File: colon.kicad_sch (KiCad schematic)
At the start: 10 parts, among them U42 SN74LVC244A

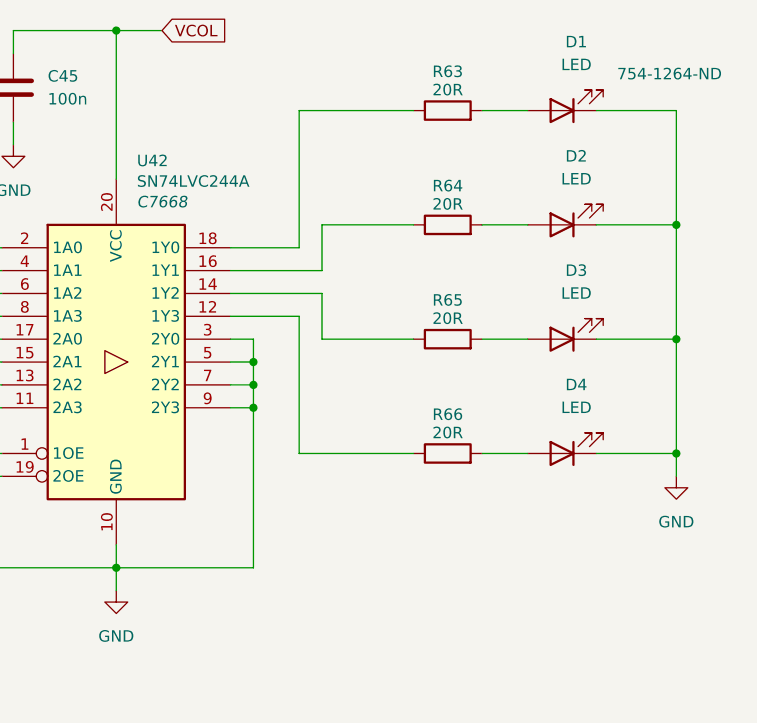
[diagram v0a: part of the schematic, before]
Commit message: buzzer addition
- reordering
- test point addition
- ferrite beads on both the MCUs
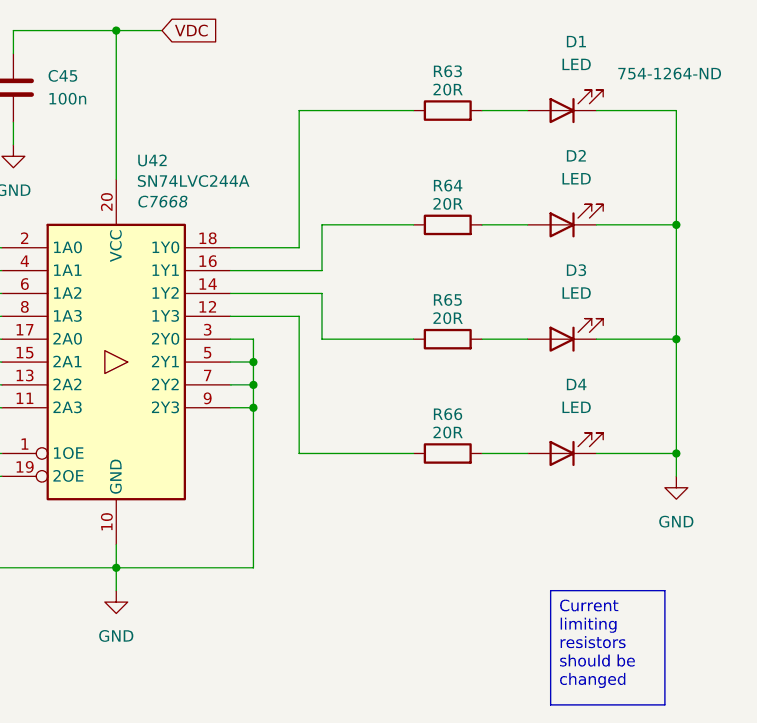
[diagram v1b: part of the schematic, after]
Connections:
- net VCOL renamed VDC
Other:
- company: (none) -> Rajath Katker
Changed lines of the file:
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@@
 	(paper "A4")
 	(title_block
-		(date "2025-10-24")
+		(date "2025-10-31")
+		(rev "v0.0")
+		(company "Rajath Katker")
+		(comment 4 "Final verification pending")
+	)
+	(text_box "Current limiting resistors should be changed"
+		(exclude_from_sim no)
+		(at 170.18 129.54 0)
+		(size 12.7 12.7)
+		(margins 0.9525 0.9525 0.9525 0.9525)
+		(stroke
+			(width 0)
+			(type solid)
+		)
+		(fill
+			(type color)
+			(color 0 255 255 1)
+		)
+		(effects
+			(font
+				(size 1.27 1.27)
+			)
+			(justify left top)
+		)
 	)
 	(junction
@@
 		)
 	)
-	(global_label "VCOL"
+	(global_label "VDC"
 		(shape input)
 		(at 127 67.31 0)
@@
 		)
 		(property "Intersheetrefs" "${INTERSHEET_REFS}"
-			(at 134.7024 67.31 0)
+			(at 133.6138 67.31 0)
 			(effects
 				(font

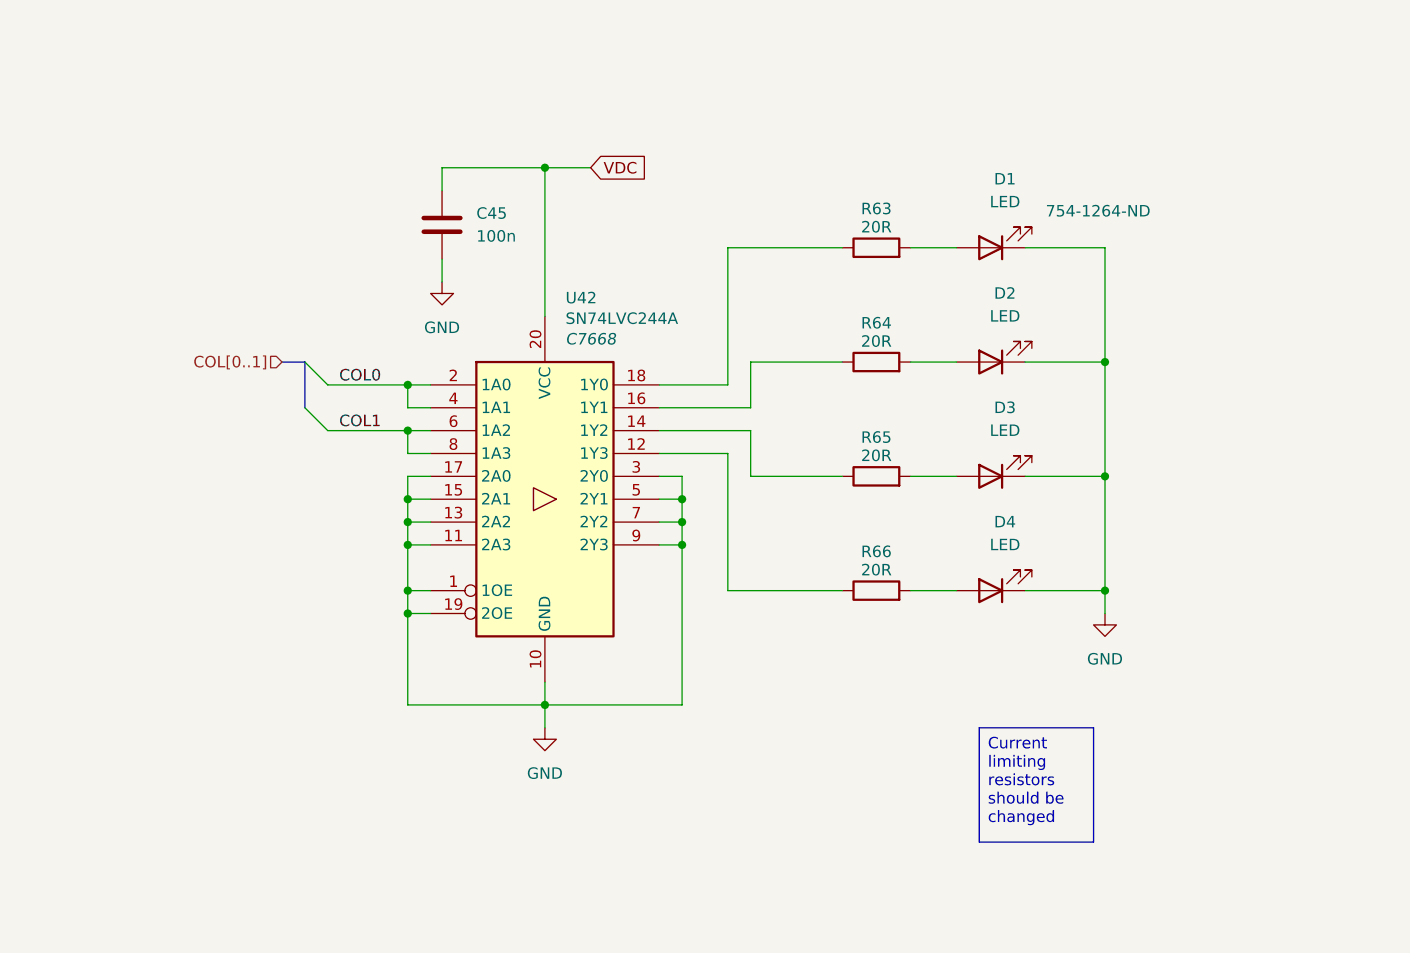
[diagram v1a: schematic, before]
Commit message: Buzzer driver added - replacement of photoresistor to a variable resistor - added button - general formatting
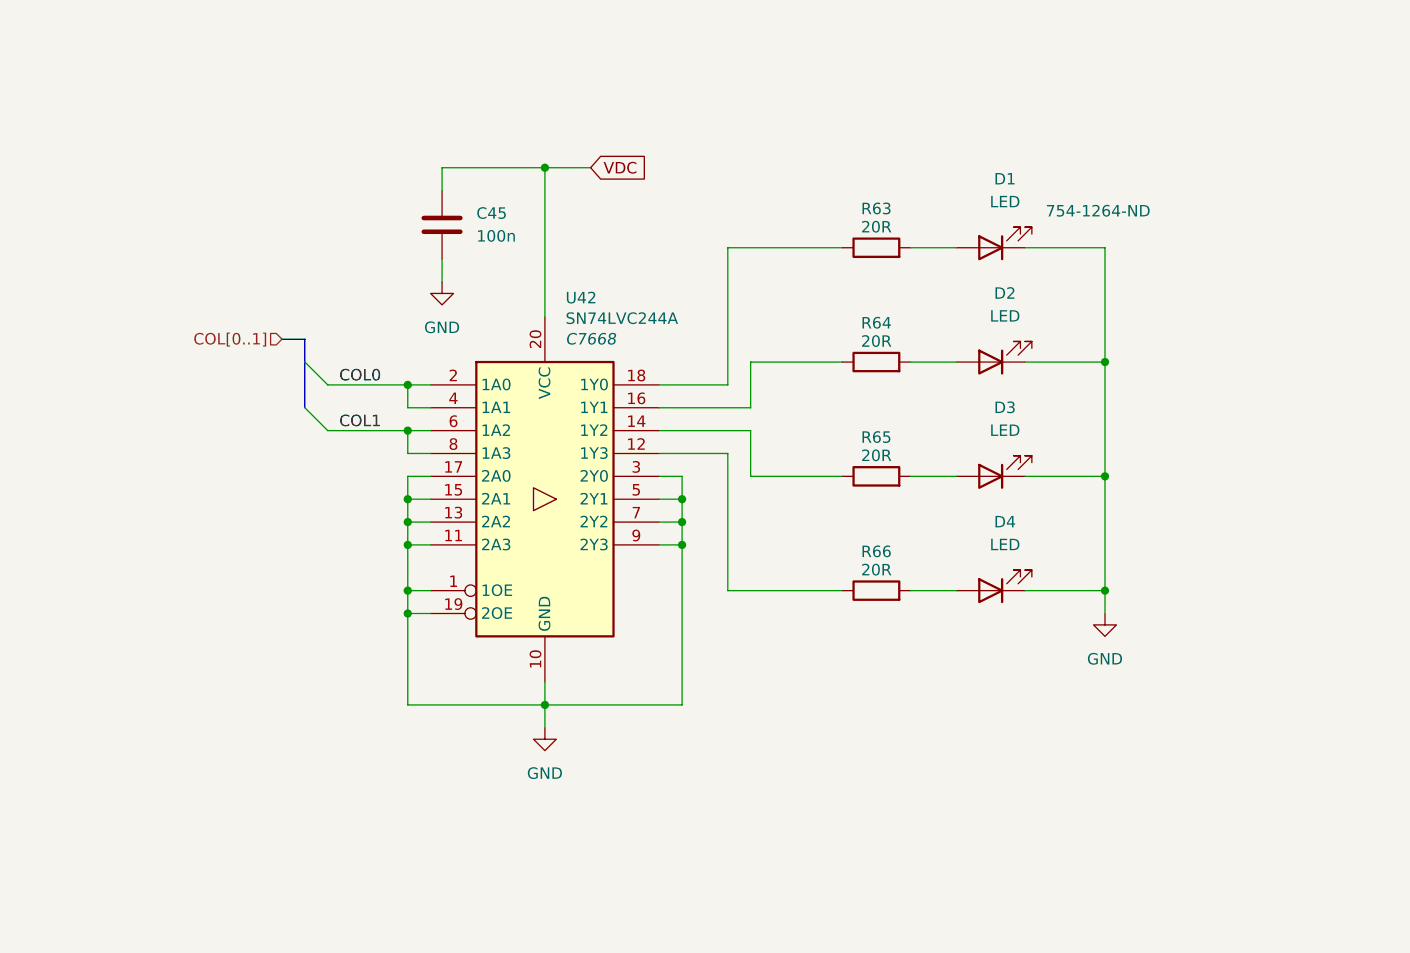
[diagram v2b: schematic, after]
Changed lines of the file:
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@@
 		(comment 4 "Final verification pending")
-	)
-	(text_box "Current limiting resistors should be changed"
-		(exclude_from_sim no)
-		(at 170.18 129.54 0)
-		(size 12.7 12.7)
-		(margins 0.9525 0.9525 0.9525 0.9525)
-		(stroke
-			(width 0)
-			(type solid)
-		)
-		(fill
-			(type color)
-			(color 0 255 255 1)
-		)
-		(effects
-			(font
-				(size 1.27 1.27)
-			)
-			(justify left top)
-		)
 	)
 	(junction
@@
 		)
 	)
+	(bus
+		(pts
+			(xy 95.25 88.9) (xy 95.25 93.98)
+		)
+		(stroke
+			(width 0)
+			(type default)
+		)
+	)
 	(wire
 		(pts
@@
 	(bus
 		(pts
-			(xy 92.71 88.9) (xy 95.25 88.9)
+			(xy 92.71 86.36) (xy 95.25 86.36)
 		)
 		(stroke
@@
 	(bus
 		(pts
-			(xy 95.25 88.9) (xy 95.25 93.98)
+			(xy 95.25 86.36) (xy 95.25 88.9)
 		)
 		(stroke
@@
 	(hierarchical_label "COL[0..1]"
 		(shape input)
-		(at 92.71 88.9 180)
+		(at 92.71 86.36 180)
 		(effects
 			(font

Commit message: ESD, LEDs, footprints
- assignment of footprints
- ESD protection
- User buttons
- addition of test points
- BOM consolidation of  resistors
- general reordering of the schematic
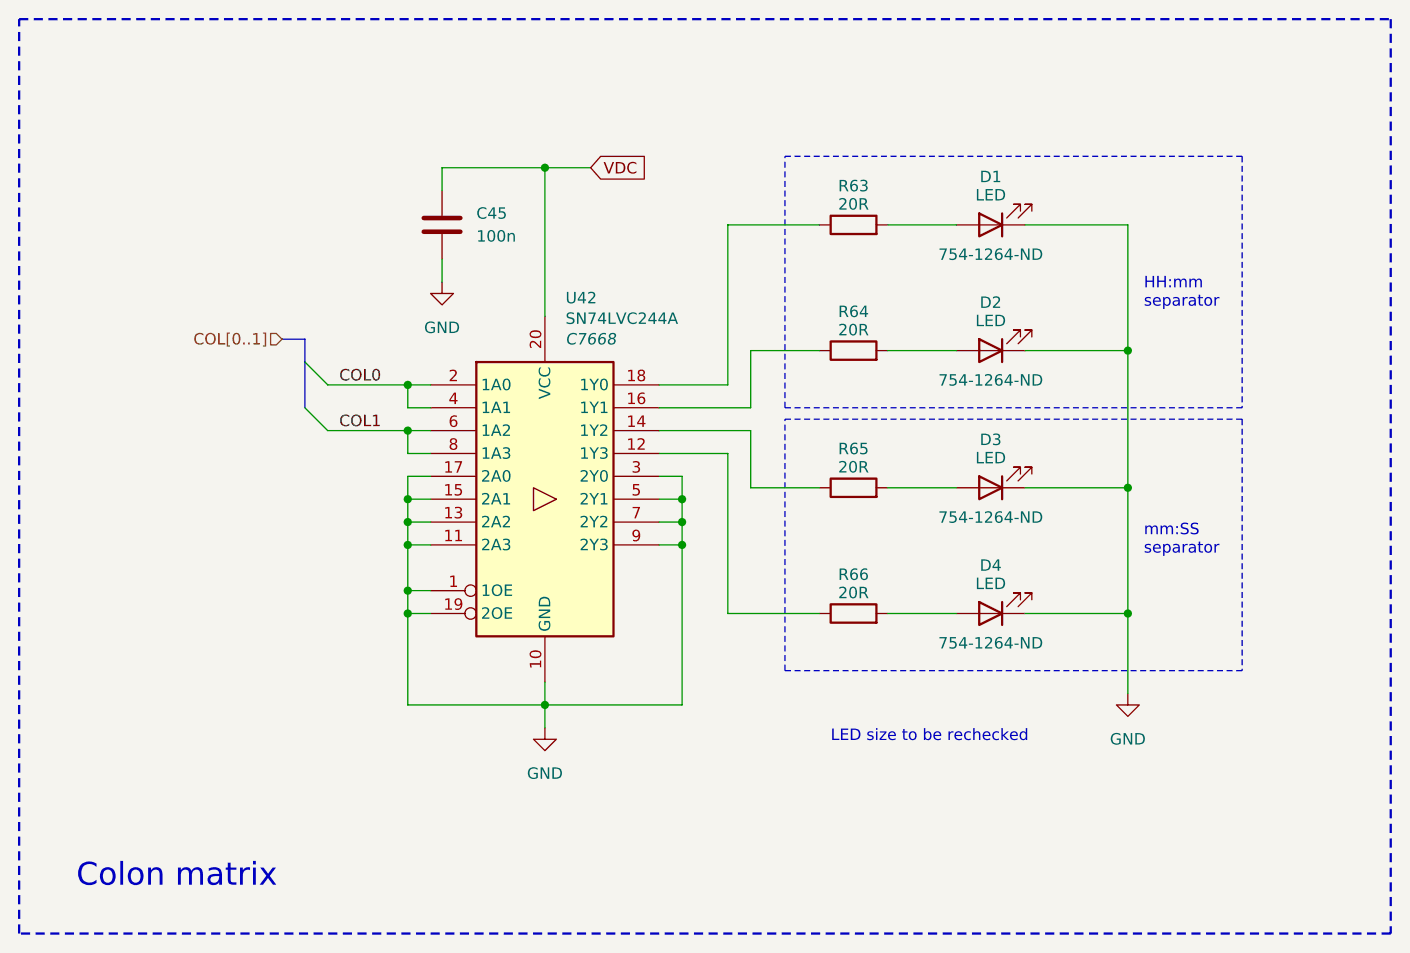
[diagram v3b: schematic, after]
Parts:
- C45: footprint (none) -> Capacitor_SMD:C_0603_1608Metric
- D2, D3, D4: Digikey (none) -> 754-1264-ND
- R63, R64, R65, R66: footprint (none) -> Resistor_SMD:R_0603_1608Metric
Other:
- note added: "Colon matrix"
- note added: "HH:mm separator"
- note added: "LED size to be rechecked"
- note added: "mm:SS separator"
- title: (none) -> Colon matrix & Driver
- moved on the sheet: D1, R63, R64, R65, R66

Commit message: verification
- sensor schematic verification
- change in the value of current limiting resistor
- disconnected unused buffer pins
- labeling or peripherals used in primary MCU
- additional user button
- DRC corrections
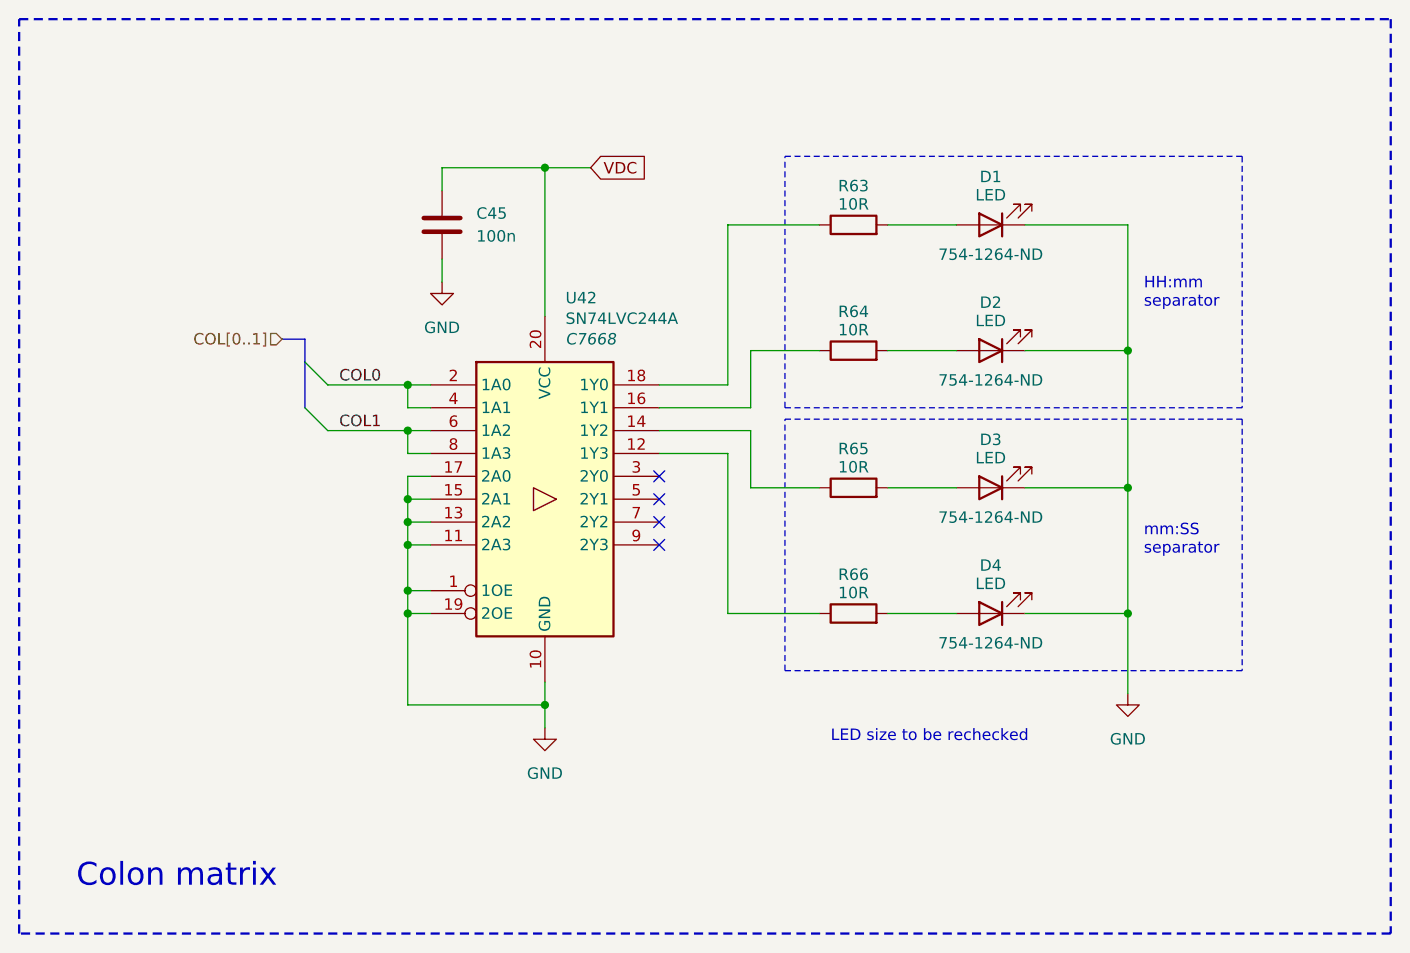
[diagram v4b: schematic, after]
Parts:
- R63, R64, R65, R66: value 20R -> 10R
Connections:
- net GND: no longer U42.3 (2Y0), U42.5 (2Y1), U42.7 (2Y2), U42.9 (2Y3)
- no-connect marks 0 -> 4
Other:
- company: Rajath Katker -> TJ71PL
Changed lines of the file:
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@@
 	(title_block
 		(title "Colon matrix & Driver")
-		(date "2025-11-04")
+		(date "2025-09-05")
 		(rev "v0.0")
-		(company "Rajath Katker")
+		(company "TJ71PL")
+		(comment 1 "天計")
 		(comment 4 "Final verification pending")
 	)
@@
 	)
 	(junction
-		(at 137.16 106.68)
-		(diameter 0)
-		(color 0 0 0 0)
-	)
-	(junction
 		(at 186.69 116.84)
 		(diameter 0)
@@
 	)
 	(junction
-		(at 137.16 109.22)
-		(diameter 0)
-		(color 0 0 0 0)
-	)
-	(junction
 		(at 106.68 104.14)
 		(diameter 0)
@@
 		(color 0 0 0 0)
 	)
-	(junction
-		(at 137.16 104.14)
-		(diameter 0)
-		(color 0 0 0 0)
+	(no_connect
+		(at 134.62 109.22)
+	)
+	(no_connect
+		(at 134.62 101.6)
+	)
+	(no_connect
+		(at 134.62 106.68)
+	)
+	(no_connect
+		(at 134.62 104.14)
 	)
 	(bus_entry
@@
 	(wire
 		(pts
-			(xy 134.62 104.14) (xy 137.16 104.14)
-		)
-		(stroke
-			(width 0)
-			(type default)
-		)
-	)
-	(wire
-		(pts
-			(xy 134.62 101.6) (xy 137.16 101.6)
-		)
-		(stroke
-			(width 0)
-			(type default)
-		)
-	)
-	(wire
-		(pts
 			(xy 106.68 104.14) (xy 106.68 106.68)
 		)
@@
 	(wire
 		(pts
-			(xy 137.16 106.68) (xy 137.16 109.22)
-		)
-		(stroke
-			(width 0)
-			(type default)
-		)
-	)
-	(wire
-		(pts
 			(xy 109.22 114.3) (xy 106.68 114.3)
 		)
@@
 	(wire
 		(pts
-			(xy 134.62 109.22) (xy 137.16 109.22)
-		)
-		(stroke
-			(width 0)
-			(type default)
-		)
-	)
-	(wire
-		(pts
 			(xy 106.68 116.84) (xy 109.22 116.84)
 		)
@@
 	(wire
 		(pts
-			(xy 121.92 127) (xy 137.16 127)
-		)
-		(stroke
-			(width 0)
-			(type default)
-		)
-	)
-	(wire
-		(pts
 			(xy 109.22 101.6) (xy 106.68 101.6)
 		)
@@
 	(wire
 		(pts
-			(xy 137.16 101.6) (xy 137.16 104.14)
-		)
-		(stroke
-			(width 0)
-			(type default)
-		)
-	)
-	(wire
-		(pts
 			(xy 144.78 87.63) (xy 152.4 87.63)
 		)
@@
 	(wire
 		(pts
-			(xy 134.62 106.68) (xy 137.16 106.68)
-		)
-		(stroke
-			(width 0)
-			(type default)
-		)
-	)
-	(wire
-		(pts
 			(xy 106.68 91.44) (xy 106.68 93.98)
 		)
@@
 	(wire
 		(pts
-			(xy 137.16 109.22) (xy 137.16 127)
-		)
-		(stroke
-			(width 0)
-			(type default)
-		)
-	)
-	(wire
-		(pts
 			(xy 144.78 96.52) (xy 134.62 96.52)
 		)
@@
 		(pts
 			(xy 106.68 91.44) (xy 109.22 91.44)
-		)
-		(stroke
-			(width 0)
-			(type default)
-		)
-	)
-	(wire
-		(pts
-			(xy 137.16 104.14) (xy 137.16 106.68)
 		)
 		(stroke
@@
 			)
 		)
-		(property "Value" "20R"
+		(property "Value" "10R"
 			(at 156.21 85.344 90)
 			(effects
@@
 			)
 		)
-		(property "Value" "20R"
+		(property "Value" "10R"
 			(at 156.21 114.554 90)
 			(effects
@@
 			)
 		)
-		(property "Value" "20R"
+		(property "Value" "10R"
 			(at 156.21 100.584 90)
 			(effects
@@
 			)
 		)
-		(property "Value" "20R"
+		(property "Value" "10R"
 			(at 156.21 71.374 90)
 			(effects

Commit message: semi final verification
- change in display type to common cathode
- verification of the schematic
- addition of footprints
- further minor changes
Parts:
- D1, D2, D3, D4: footprint (none) -> LED_THT:LED_D5.0mm
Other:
- note removed: "LED size to be rechecked"
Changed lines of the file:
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@@
 	(title_block
 		(title "Colon matrix & Driver")
-		(date "2025-09-05")
+		(date "2025-11-07")
 		(rev "v0.0")
 		(company "TJ71PL")
 		(comment 1 "天計")
-		(comment 4 "Final verification pending")
+		(comment 4 "Final verification complete")
 	)
 	(rectangle
@@
 				(size 1.27 1.27)
 				(color 132 0 0 1)
-			)
-			(justify left)
-		)
-	)
-	(text "LED size to be rechecked"
-		(exclude_from_sim no)
-		(at 153.67 130.556 0)
-		(effects
-			(font
-				(size 1.27 1.27)
 			)
 			(justify left)
@@
 			)
 		)
-		(property "Footprint" ""
+		(property "Footprint" "LED_THT:LED_D5.0mm"
 			(at 171.45 73.66 0)
 			(effects
@@
 			)
 		)
-		(property "Footprint" ""
+		(property "Footprint" "LED_THT:LED_D5.0mm"
 			(at 171.45 102.87 0)
 			(effects
@@
 			)
 		)
-		(property "Footprint" ""
+		(property "Footprint" "LED_THT:LED_D5.0mm"
 			(at 171.45 116.84 0)
 			(effects
@@
 			)
 		)
-		(property "Footprint" ""
+		(property "Footprint" "LED_THT:LED_D5.0mm"
 			(at 171.45 87.63 0)
 			(effects
